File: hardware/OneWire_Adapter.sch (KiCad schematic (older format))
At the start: 7 parts, among them T1 BC547, T2 BC547, X1 USART, X2 1-Wire

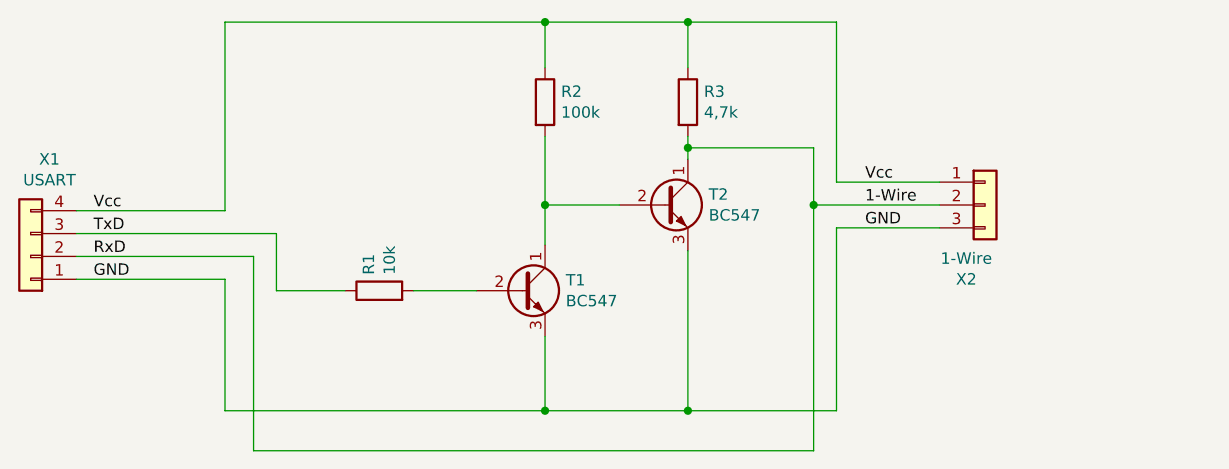
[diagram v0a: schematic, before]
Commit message: Add level shifter
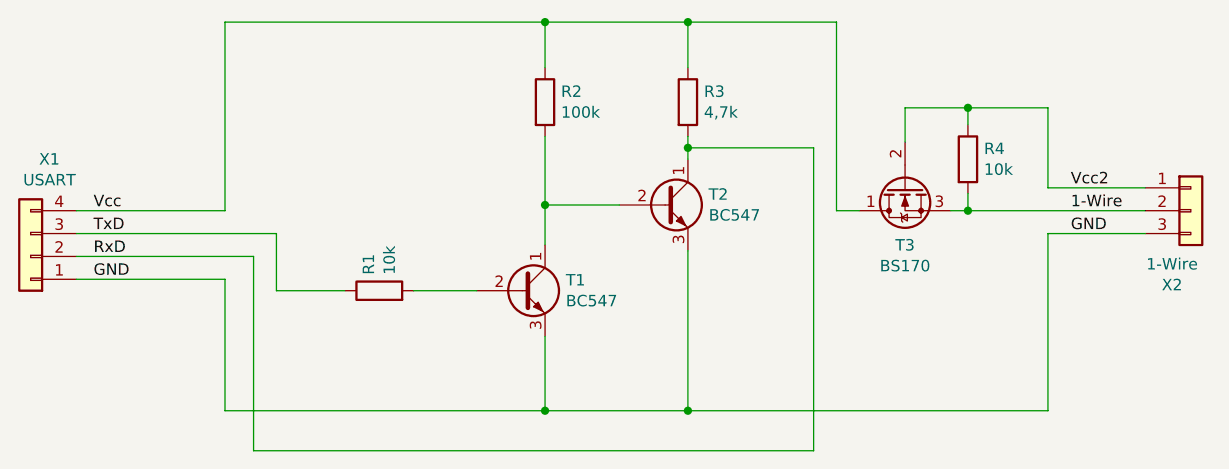
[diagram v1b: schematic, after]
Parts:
- added R4: 10k, Resistor_THT:R_Axial_DIN0207_L6.3mm_D2.5mm_P10.16mm_Horizontal, symbol Device:R
- added T3: BS170, Package_TO_SOT_THT:TO-92_Inline, symbol Transistor_FET:BS170
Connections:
- net 1-Wire: now also R4.2, T3.3 (S); no longer R3.2, T2.1 (C), X1.2 (Pin_2)
- net Vcc: now also T3.1 (D); no longer X2.1 (Pin_1)
- new net RxD: R3.2, T2.1 (C), X1.2 (Pin_2)
- new net Vcc2: R4.1, T3.2 (G), X2.1 (Pin_1)
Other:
- moved on the sheet: X2
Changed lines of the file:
@@
 L Connector_Generic:Conn_01x03 X2
 U 1 1 5E315D1F
-P 10300 5525
-F 0 "X2" H 10218 5200 50  0000 C CNN
-F 1 "1-Wire" H 10218 5291 50  0000 C CNN
-F 2 "Connector_PinHeader_2.54mm:PinHeader_1x03_P2.54mm_Horizontal" H 10300 5525 50  0001 C CNN
-F 3 "https://www.mouser.de/datasheet/2/181/M20-977-1220590.pdf" H 10300 5525 50  0001 C CNN
-F 4 "Harwin" H 10300 5525 50  0001 C CNN "Mfr."
-F 5 "M20-9750346" H 10300 5525 50  0001 C CNN "Mfr. No."
-F 6 "855-M20-9750346" H 10300 5525 50  0001 C CNN "Mouser"
-	1    10300 5525
+P 11200 5550
+F 0 "X2" H 11118 5225 50  0000 C CNN
+F 1 "1-Wire" H 11118 5316 50  0000 C CNN
+F 2 "Connector_PinHeader_2.54mm:PinHeader_1x03_P2.54mm_Horizontal" H 11200 5550 50  0001 C CNN
+F 3 "https://www.mouser.de/datasheet/2/181/M20-977-1220590.pdf" H 11200 5550 50  0001 C CNN
+F 4 "Harwin" H 11200 5550 50  0001 C CNN "Mfr."
+F 5 "M20-9750346" H 11200 5550 50  0001 C CNN "Mfr. No."
+F 6 "855-M20-9750346" H 11200 5550 50  0001 C CNN "Mouser"
+	1    11200 5550
 	1    0    0    -1
 $EndComp
@@
 Wire Wire Line
 	9000 5275 9550 5275
-Wire Wire Line
-	9550 5275 9550 5525
-Wire Wire Line
-	9550 5525 10100 5525
 Connection ~ 9000 5275
 Wire Wire Line
 	9000 5275 9000 5325
-Wire Wire Line
-	9550 5525 9550 6600
-Connection ~ 9550 5525
 Wire Wire Line
 	7500 5900 7200 5900
@@
 	6975 5850 6325 5850
 Connection ~ 8375 6425
-Wire Wire Line
-	9000 6425 9650 6425
-Wire Wire Line
-	9650 6425 9650 5625
-Wire Wire Line
-	9650 5625 10100 5625
 Connection ~ 9000 6425
 Wire Wire Line
 	9000 4725 9650 4725
-Wire Wire Line
-	9650 4725 9650 5425
-Wire Wire Line
-	9650 5425 10100 5425
 Connection ~ 9000 4725
 Wire Wire Line
@@
 Text Label 6400 5550 0    50   ~ 0
 Vcc
-Text Label 9775 5425 0    50   ~ 0
-Vcc
-Text Label 9775 5625 0    50   ~ 0
+Text Label 10675 5450 0    50   ~ 0
+Vcc2
+Text Label 10675 5650 0    50   ~ 0
 GND
-Text Label 9775 5525 0    50   ~ 0
+Text Label 10675 5550 0    50   ~ 0
 1-Wire
+Wire Wire Line
+	9550 5275 9550 6600
+$Comp
+L Transistor_FET:BS170 T3
+U 1 1 5E31EDCD
+P 9950 5450
+F 0 "T3" V 10201 5450 50  0000 C CNN
+F 1 "BS170" V 10292 5450 50  0000 C CNN
+F 2 "Package_TO_SOT_THT:TO-92_Inline" H 10150 5375 50  0001 L CIN
+F 3 "http://www.fairchildsemi.com/ds/BS/BS170.pdf" H 9950 5450 50  0001 L CNN
+F 4 "ON Semiconductor / Fairchild" H 9950 5450 50  0001 C CNN "Mfr."
+F 5 "BS170" H 9950 5450 50  0001 C CNN "Mfr. No."
+F 6 "512-BS170" H 9950 5450 50  0001 C CNN "Mouser"
+	1    9950 5450
+	0    -1   1    0
+$EndComp
+Wire Wire Line
+	9750 5550 9650 5550
+Wire Wire Line
+	9650 4725 9650 5550
+Wire Wire Line
+	10575 5650 10575 6425
+Wire Wire Line
+	10575 5650 11000 5650
+Wire Wire Line
+	9000 6425 10575 6425
+$Comp
+L Device:R R4
+U 1 1 5E32490F
+P 10225 5325
+F 0 "R4" H 10295 5371 50  0000 L CNN
+F 1 "10k" H 10295 5280 50  0000 L CNN
+F 2 "Resistor_THT:R_Axial_DIN0207_L6.3mm_D2.5mm_P10.16mm_Horizontal" V 10155 5325 50  0001 C CNN
+F 3 "https://www.mouser.de/datasheet/2/447/Yageo%20LR_MFR_2013-467719.pdf" H 10225 5325 50  0001 C CNN
+F 4 "Yageo" H 10225 5325 50  0001 C CNN "Mfr."
+F 5 "MFR-25FBF52-10K" H 10225 5325 50  0001 C CNN "Mfr. No."
+F 6 "603-MFR-25FBF52-10K" H 10225 5325 50  0001 C CNN "Mouser"
+	1    10225 5325
+	1    0    0    -1
+$EndComp
+Wire Wire Line
+	10150 5550 10225 5550
+Wire Wire Line
+	10225 5475 10225 5550
+Connection ~ 10225 5550
+Wire Wire Line
+	10225 5550 11000 5550
+Wire Wire Line
+	9950 5250 9950 5100
+Wire Wire Line
+	9950 5100 10225 5100
+Wire Wire Line
+	10225 5100 10225 5175
+Wire Wire Line
+	10225 5100 10575 5100
+Wire Wire Line
+	10575 5100 10575 5450
+Connection ~ 10225 5100
+Wire Wire Line
+	10575 5450 11000 5450
 $EndSCHEMATC

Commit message: Add new schematics
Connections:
- net RxD: now also T3.1 (D)
- net Vcc renamed VH
- net VH: no longer T3.1 (D)
- net Vcc2 renamed VL
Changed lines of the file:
@@
-$EndComp
-$Comp
-L Device:R R1
-U 1 1 5E3148B5
-P 7650 5900
-F 0 "R1" H 7720 5946 50  0000 L CNN
-F 1 "10k" H 7720 5855 50  0000 L CNN
-F 2 "Resistor_THT:R_Axial_DIN0207_L6.3mm_D2.5mm_P10.16mm_Horizontal" V 7580 5900 50  0001 C CNN
-F 3 "https://www.mouser.de/datasheet/2/447/Yageo%20LR_MFR_2013-467719.pdf" H 7650 5900 50  0001 C CNN
-F 4 "Yageo" H 7650 5900 50  0001 C CNN "Mfr."
-F 5 "MFR-25FBF52-10K" H 7650 5900 50  0001 C CNN "Mfr. No."
-F 6 "603-MFR-25FBF52-10K" H 7650 5900 50  0001 C CNN "Mouser"
-	1    7650 5900
-	0    -1   -1   0
 $EndComp
 $Comp
@@
 Connection ~ 9000 6425
 Wire Wire Line
-	9000 4725 9650 4725
-Connection ~ 9000 4725
-Wire Wire Line
 	6325 5550 6975 5550
 Wire Wire Line
@@
 GND
 Text Label 6400 5550 0    50   ~ 0
-Vcc
+VH
 Text Label 10675 5450 0    50   ~ 0
-Vcc2
+VL
 Text Label 10675 5650 0    50   ~ 0
 GND
@@
 1-Wire
 Wire Wire Line
-	9550 5275 9550 6600
+	9550 5275 9550 5550
 $Comp
 L Transistor_FET:BS170 T3
@@
 $EndComp
 Wire Wire Line
-	9750 5550 9650 5550
-Wire Wire Line
-	9650 4725 9650 5550
-Wire Wire Line
 	10575 5650 10575 6425
 Wire Wire Line
@@
 Wire Wire Line
 	10575 5450 11000 5450
+$Comp
+L Device:R R1
+U 1 1 5E3148B5
+P 7650 5900
+F 0 "R1" V 7550 5925 50  0000 C CNN
+F 1 "10k" V 7450 5900 50  0000 C CNN
+F 2 "Resistor_THT:R_Axial_DIN0207_L6.3mm_D2.5mm_P10.16mm_Horizontal" V 7580 5900 50  0001 C CNN
+F 3 "https://www.mouser.de/datasheet/2/447/Yageo%20LR_MFR_2013-467719.pdf" H 7650 5900 50  0001 C CNN
+F 4 "Yageo" H 7650 5900 50  0001 C CNN "Mfr."
+F 5 "MFR-25FBF52-10K" H 7650 5900 50  0001 C CNN "Mfr. No."
+F 6 "603-MFR-25FBF52-10K" H 7650 5900 50  0001 C CNN "Mouser"
+	1    7650 5900
+	0    -1   -1   0
+$EndComp
+Wire Wire Line
+	9550 5550 9750 5550
+Connection ~ 9550 5550
+Wire Wire Line
+	9550 5550 9550 6600
 $EndSCHEMATC
